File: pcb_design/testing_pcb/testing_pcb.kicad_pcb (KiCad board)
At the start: 2 copper layers, 60 x 60 mm, 56 parts, among them J10 SOx, J11 Conn_01x04_Pin, J12 Conn_01x04_Pin, J2 ST-LINK Flasher, J3 batt_1x2, J5 INH/Lx, J6 gnd, J7 V, J8 out, U1 STM32G431CBTx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

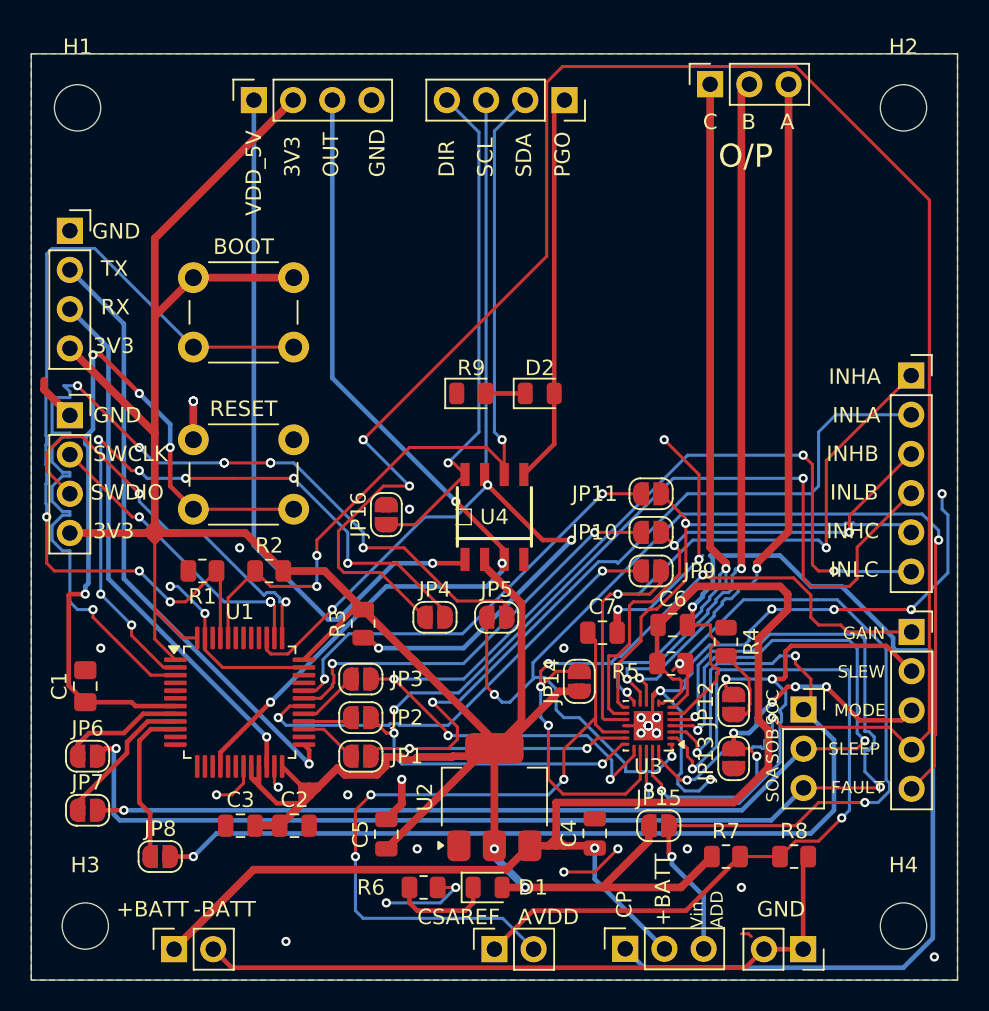
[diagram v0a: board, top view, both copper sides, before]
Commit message: added round corners , fixed acute angle turns
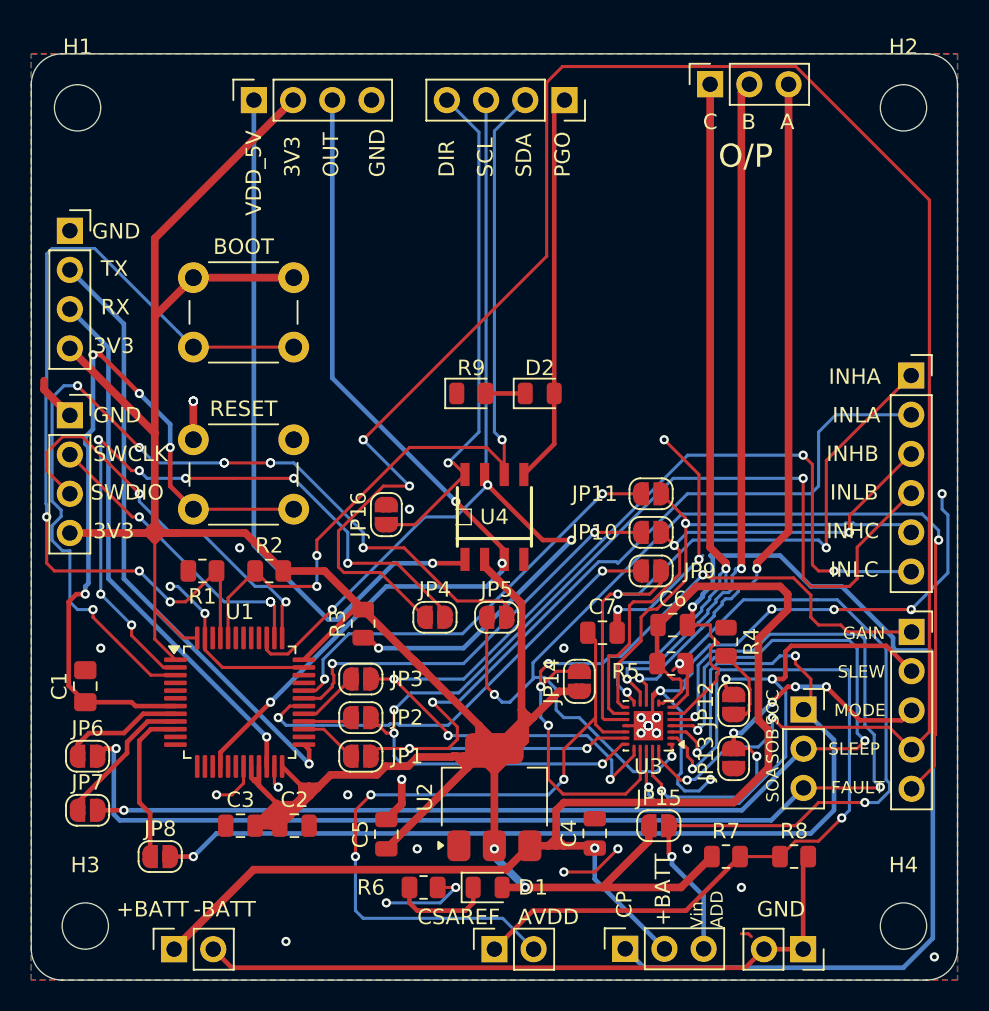
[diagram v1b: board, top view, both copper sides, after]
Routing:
- net +3V3: track 197.6 -> 223.4 mm
- net Net-(JP5-B): track 66.0 -> 60.6 mm
- net /SOA: track 84.6 -> 83.7 mm
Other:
- outline, holes or cut-outs redrawn
